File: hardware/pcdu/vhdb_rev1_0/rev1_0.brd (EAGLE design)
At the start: 100 x 40 mm, 69 parts, among them J1 AJP92A8813, J2 AJP92A8813, J3 AJP92A8813, J4 AJP92A8813, J5 AJP92A8813, Q1 25MHz, SW1 KSZ9897RTXC

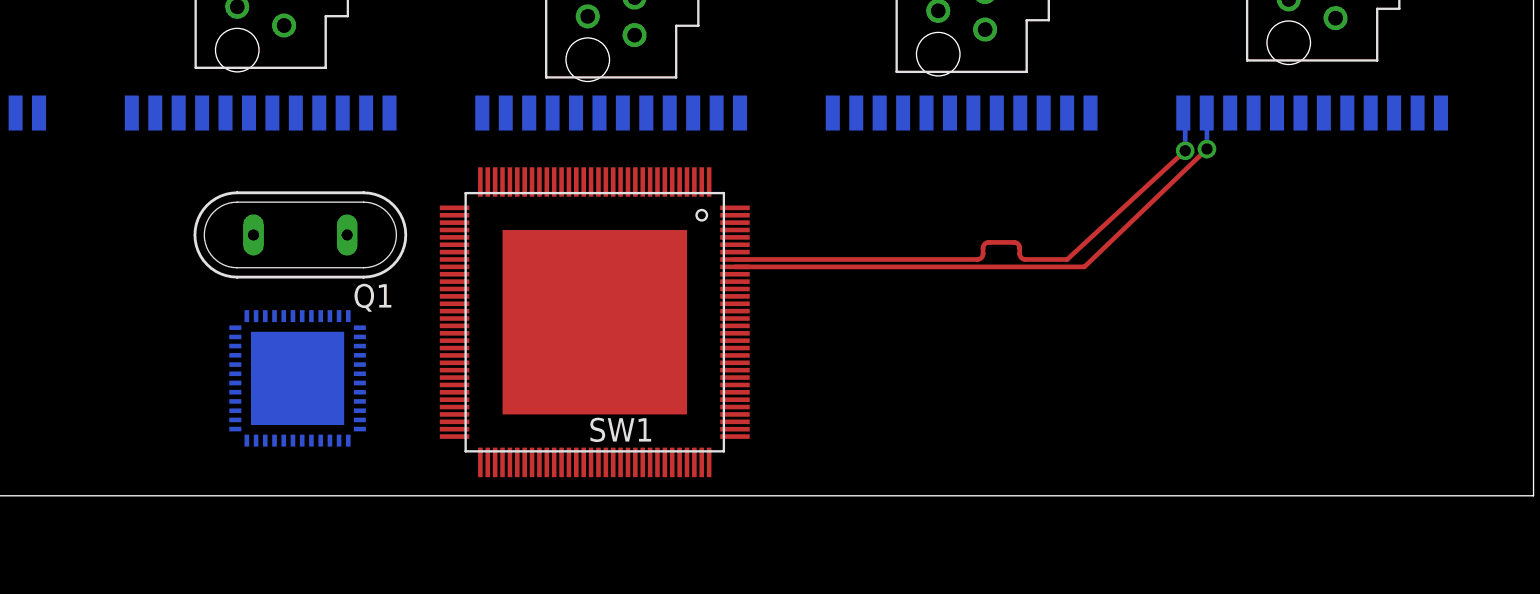
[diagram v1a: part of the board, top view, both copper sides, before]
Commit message: Minor changes to high density board
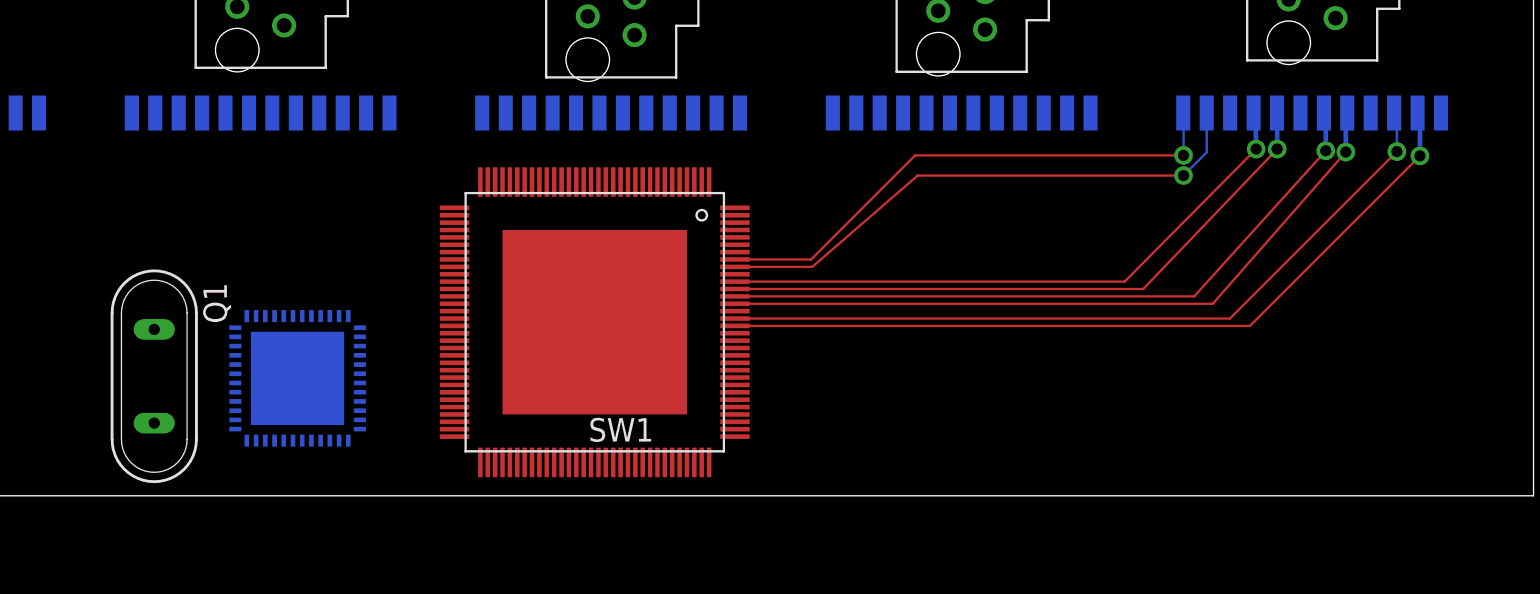
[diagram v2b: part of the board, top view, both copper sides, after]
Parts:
- moved Q1 11.0 mm to (25.2, 6.48), turned to 270 degrees
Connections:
- net N$38 renamed D53_N
- net N$39 renamed D53_P
- net N$40 renamed D52_N
- net N$41 renamed D52_P
- net N$42 renamed D51_N
- net N$43 renamed D51_P
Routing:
- net D51_P: track 0.00 -> 43.3 mm, vias 0 -> 1
- net D51_N: track 0.00 -> 41.8 mm, vias 0 -> 1
- net D52_P: track 0.00 -> 39.0 mm, vias 0 -> 1
- net D52_N: track 0.00 -> 37.6 mm, vias 0 -> 1
- net D53_P: track 0.00 -> 34.7 mm, vias 0 -> 1
- net D53_N: track 0.00 -> 33.2 mm, vias 0 -> 1
- net D54_N: track 29.9 -> 29.0 mm
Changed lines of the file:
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@@
 <class number="0" name="default" width="0" drill="0">
 </class>
+<class number="1" name="diff" width="0.127" drill="0.3">
+<clearance class="0" value="0.508"/>
+<clearance class="1" value="0.127"/>
+</class>
 </classes>
-<designrules name="default">
+<designrules name="default *">
 <description language="de">&lt;b&gt;EAGLE Design Rules&lt;/b&gt;
 &lt;p&gt;
@@
 <param name="mdDrill" value="8mil"/>
 <param name="mdSmdStop" value="0mil"/>
-<param name="msWidth" value="10mil"/>
+<param name="msWidth" value="5mil"/>
 <param name="msDrill" value="24mil"/>
 <param name="msMicroVia" value="9.99mm"/>
@@
 <element name="J4" library="AJP92A8813" package="AJP92A8813" value="AJP92A8813" x="12" y="28.75" rot="R270"/>
 <element name="J5" library="AJP92A8813" package="AJP92A8813" value="AJP92A8813" x="88" y="29.45" rot="R270"/>
-<element name="Q1" library="special" package="QS" value="25MHz" x="33.15" y="14.14" rot="R180"/>
+<element name="Q1" library="special" package="QS" value="25MHz" x="25.23" y="6.48" rot="R270"/>
 <element name="R1" library="resistor" package="R0805" value="10K" x="-40.64" y="41.91"/>
 <element name="R2" library="resistor" package="R0805" value="6.04kΩ" x="-52.07" y="33.02"/>
@@
 <contactref element="PHY2" pad="XI"/>
 <wire x1="31.25" y1="2.99" x2="56.71" y2="14.81" width="0" layer="19" extent="1-16"/>
-<wire x1="30.61" y1="14.14" x2="31.25" y2="2.99" width="0" layer="19" extent="16-16"/>
-<wire x1="-56.83" y1="52.07" x2="30.61" y2="14.14" width="0" layer="19" extent="1-1"/>
+<wire x1="25.23" y1="3.94" x2="31.25" y2="2.99" width="0" layer="19" extent="16-16"/>
+<wire x1="-56.83" y1="52.07" x2="25.23" y2="3.94" width="0" layer="19" extent="1-1"/>
 </signal>
 <signal name="XO">
@@
 <contactref element="Q1" pad="1"/>
 <contactref element="C34" pad="1"/>
-<wire x1="35.69" y1="14.14" x2="56.71" y2="14.41" width="0" layer="19" extent="1-1"/>
-<wire x1="-61.91" y1="52.07" x2="35.69" y2="14.14" width="0" layer="19" extent="1-1"/>
+<wire x1="25.23" y1="9.02" x2="56.71" y2="14.41" width="0" layer="19" extent="1-1"/>
+<wire x1="-61.91" y1="52.07" x2="25.23" y2="9.02" width="0" layer="19" extent="1-1"/>
 </signal>
 <signal name="MODE0">
@@
 <wire x1="24.015" y1="20.75" x2="42.91" y2="17.01" width="0" layer="19" extent="1-16"/>
 </signal>
-<signal name="D54_N">
+<signal name="D54_N" class="1">
 <contactref element="SW1" pad="TXRX5M_D"/>
 <contactref element="MAG5" pad="TD4-"/>
-<wire x1="74.71670625" y1="12.81" x2="72.45695" y2="12.81" width="0.254" layer="1"/>
-<wire x1="72.45695" y1="12.81" x2="72.14745" y2="13.1195" width="0.254" layer="1" curve="-90"/>
-<wire x1="72.14745" y1="13.1195" x2="72.14745" y2="13.426025" width="0.254" layer="1"/>
-<wire x1="72.14745" y1="13.426025" x2="71.83795" y2="13.735525" width="0.254" layer="1" curve="90"/>
-<wire x1="71.83795" y1="13.735525" x2="70.469" y2="13.735525" width="0.254" layer="1"/>
-<wire x1="70.469" y1="13.735525" x2="70.1595" y2="13.426025" width="0.254" layer="1" curve="90"/>
-<wire x1="70.1595" y1="13.426025" x2="70.1595" y2="13.1195" width="0.254" layer="1"/>
-<wire x1="70.1595" y1="13.1195" x2="69.85" y2="12.81" width="0.254" layer="1" curve="-90"/>
-<wire x1="69.85" y1="12.81" x2="56.71" y2="12.81" width="0.254" layer="1"/>
-<wire x1="74.71670625" y1="12.81" x2="81.118353125" y2="18.703646875" width="0.254" layer="1"/>
-<via x="81.118353125" y="18.703646875" extent="1-16" drill="0.6096"/>
-<wire x1="81.118353125" y1="18.703646875" x2="81.118353125" y2="20.646646875" width="0.254" layer="16"/>
-<wire x1="81.118353125" y1="20.646646875" x2="81.015" y2="20.75" width="0.254" layer="16"/>
-</signal>
-<signal name="D54_P">
+<wire x1="56.71" y1="12.81" x2="60.8365125" y2="12.81" width="0.127" layer="1"/>
+<wire x1="60.8365125" y1="12.81" x2="66.4796125" y2="18.4531" width="0.127" layer="1"/>
+<wire x1="66.4796125" y1="18.4531" x2="81.026" y2="18.4531" width="0.127" layer="1"/>
+<via x="81.026" y="18.4531" extent="1-16" drill="0.6096"/>
+<wire x1="81.026" y1="18.4531" x2="81.026" y2="20.739" width="0.127" layer="16"/>
+<wire x1="81.026" y1="20.739" x2="81.015" y2="20.75" width="0.127" layer="16"/>
+</signal>
+<signal name="D54_P" class="1">
 <contactref element="SW1" pad="TXRX5P_D"/>
 <contactref element="MAG5" pad="TD4+"/>
-<wire x1="75.656" y1="12.41" x2="56.71" y2="12.41" width="0.254" layer="1"/>
-<via x="82.296" y="18.796" extent="1-16" drill="0.6096"/>
-<wire x1="82.296" y1="18.796" x2="82.296" y2="20.739" width="0.254" layer="16"/>
-<wire x1="82.296" y1="20.739" x2="82.285" y2="20.75" width="0.254" layer="16"/>
-<wire x1="75.656" y1="12.41" x2="82.296" y2="18.796" width="0.254" layer="1"/>
-</signal>
-<signal name="N$38">
+<wire x1="56.71" y1="12.41" x2="60.9034875" y2="12.41" width="0.127" layer="1"/>
+<wire x1="60.9034875" y1="12.41" x2="66.6163875" y2="17.3609" width="0.127" layer="1"/>
+<wire x1="66.6163875" y1="17.3609" x2="81.026" y2="17.3609" width="0.127" layer="1"/>
+<via x="81.026" y="17.3609" extent="1-16" drill="0.6096"/>
+<wire x1="81.026" y1="17.3609" x2="82.285" y2="18.6199" width="0.127" layer="16"/>
+<wire x1="82.285" y1="18.6199" x2="82.285" y2="20.75" width="0.127" layer="16"/>
+</signal>
+<signal name="D53_N" class="1">
 <contactref element="SW1" pad="TXRX5M_C"/>
 <contactref element="MAG5" pad="TD3-"/>
-<wire x1="56.71" y1="11.61" x2="84.825" y2="20.75" width="0" layer="19" extent="1-16"/>
-</signal>
-<signal name="N$39">
+<wire x1="56.71" y1="11.61" x2="77.83470625" y2="11.61" width="0.127" layer="1"/>
+<wire x1="84.963" y1="18.796" x2="77.83470625" y2="11.61" width="0.127" layer="1"/>
+<via x="84.963" y="18.796" extent="1-16" drill="0.6096"/>
+<wire x1="84.963" y1="18.796" x2="84.928353125" y2="20.646646875" width="0.254" layer="16"/>
+<wire x1="84.928353125" y1="20.646646875" x2="84.825" y2="20.75" width="0.254" layer="16"/>
+</signal>
+<signal name="D53_P" class="1">
 <contactref element="SW1" pad="TXRX5P_C"/>
 <contactref element="MAG5" pad="TD3+"/>
-<wire x1="56.71" y1="11.21" x2="86.095" y2="20.75" width="0" layer="19" extent="1-16"/>
-</signal>
-<signal name="N$40">
+<wire x1="56.71" y1="11.21" x2="78.84329375" y2="11.21" width="0.127" layer="1"/>
+<wire x1="78.84329375" y1="11.21" x2="86.106" y2="18.796" width="0.127" layer="1"/>
+<via x="86.106" y="18.796" extent="1-16" drill="0.6096"/>
+<wire x1="86.013646875" y1="20.668646875" x2="86.095" y2="20.75" width="0.254" layer="16"/>
+<wire x1="86.106" y1="18.796" x2="86.106" y2="20.739" width="0.254" layer="16"/>
+<wire x1="86.106" y1="20.739" x2="86.095" y2="20.75" width="0.254" layer="16"/>
+</signal>
+<signal name="D52_N" class="1">
 <contactref element="SW1" pad="TXRX5M_B"/>
 <contactref element="MAG5" pad="TD2-"/>
-<wire x1="56.71" y1="10.81" x2="88.635" y2="20.75" width="0" layer="19" extent="1-16"/>
-</signal>
-<signal name="N$41">
+<wire x1="56.71" y1="10.81" x2="81.60670625" y2="10.81" width="0.127" layer="1"/>
+<wire x1="81.60670625" y1="10.81" x2="88.738353125" y2="18.703646875" width="0.127" layer="1"/>
+<via x="88.738353125" y="18.703646875" extent="1-16" drill="0.6096"/>
+<wire x1="88.738353125" y1="18.703646875" x2="88.738353125" y2="20.646646875" width="0.254" layer="16"/>
+<wire x1="88.738353125" y1="20.646646875" x2="88.635" y2="20.75" width="0.254" layer="16"/>
+</signal>
+<signal name="D52_P" class="1">
 <contactref element="SW1" pad="TXRX5P_B"/>
 <contactref element="MAG5" pad="TD2+"/>
-<wire x1="56.71" y1="10.41" x2="89.905" y2="20.75" width="0" layer="19" extent="1-16"/>
-</signal>
-<signal name="N$42">
+<wire x1="56.71" y1="10.41" x2="82.61529375" y2="10.41" width="0.127" layer="1"/>
+<wire x1="82.61529375" y1="10.41" x2="89.823646875" y2="18.634353125" width="0.127" layer="1"/>
+<via x="89.823646875" y="18.634353125" extent="1-16" drill="0.6096"/>
+<wire x1="89.823646875" y1="18.634353125" x2="89.823646875" y2="20.668646875" width="0.254" layer="16"/>
+<wire x1="89.823646875" y1="20.668646875" x2="89.905" y2="20.75" width="0.254" layer="16"/>
+</signal>
+<signal name="D51_N" class="1">
 <contactref element="SW1" pad="TXRX5M_A"/>
 <contactref element="MAG5" pad="TD1-"/>
-<wire x1="56.71" y1="9.61" x2="92.445" y2="20.75" width="0" layer="19" extent="1-16"/>
-</signal>
-<signal name="N$43">
+<wire x1="56.71" y1="9.61" x2="83.5445125" y2="9.61" width="0.127" layer="1"/>
+<wire x1="83.5445125" y1="9.61" x2="92.59325625" y2="18.65874375" width="0.127" layer="1"/>
+<via x="92.59325625" y="18.65874375" extent="1-16" drill="0.6096"/>
+<wire x1="92.59325625" y1="18.65874375" x2="92.59325625" y2="20.60174375" width="0.127" layer="16"/>
+<wire x1="92.59325625" y1="20.60174375" x2="92.445" y2="20.75" width="0.127" layer="16"/>
+</signal>
+<signal name="D51_P" class="1">
 <contactref element="SW1" pad="TXRX5P_A"/>
 <contactref element="MAG5" pad="TD1+"/>
-<wire x1="56.71" y1="9.21" x2="93.715" y2="20.75" width="0" layer="19" extent="1-16"/>
+<wire x1="56.71" y1="9.21" x2="84.6274875" y2="9.21" width="0.127" layer="1"/>
+<wire x1="84.6274875" y1="9.21" x2="93.84274375" y2="18.42525625" width="0.127" layer="1"/>
+<via x="93.84274375" y="18.42525625" extent="1-16" drill="0.6096"/>
+<wire x1="93.84274375" y1="18.42525625" x2="93.84274375" y2="20.62225625" width="0.254" layer="16"/>
+<wire x1="93.84274375" y1="20.62225625" x2="93.715" y2="20.75" width="0.254" layer="16"/>
 </signal>
 <signal name="N$44">
